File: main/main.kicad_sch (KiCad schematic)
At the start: 5 parts, among them SW1 SW_DPST_x2

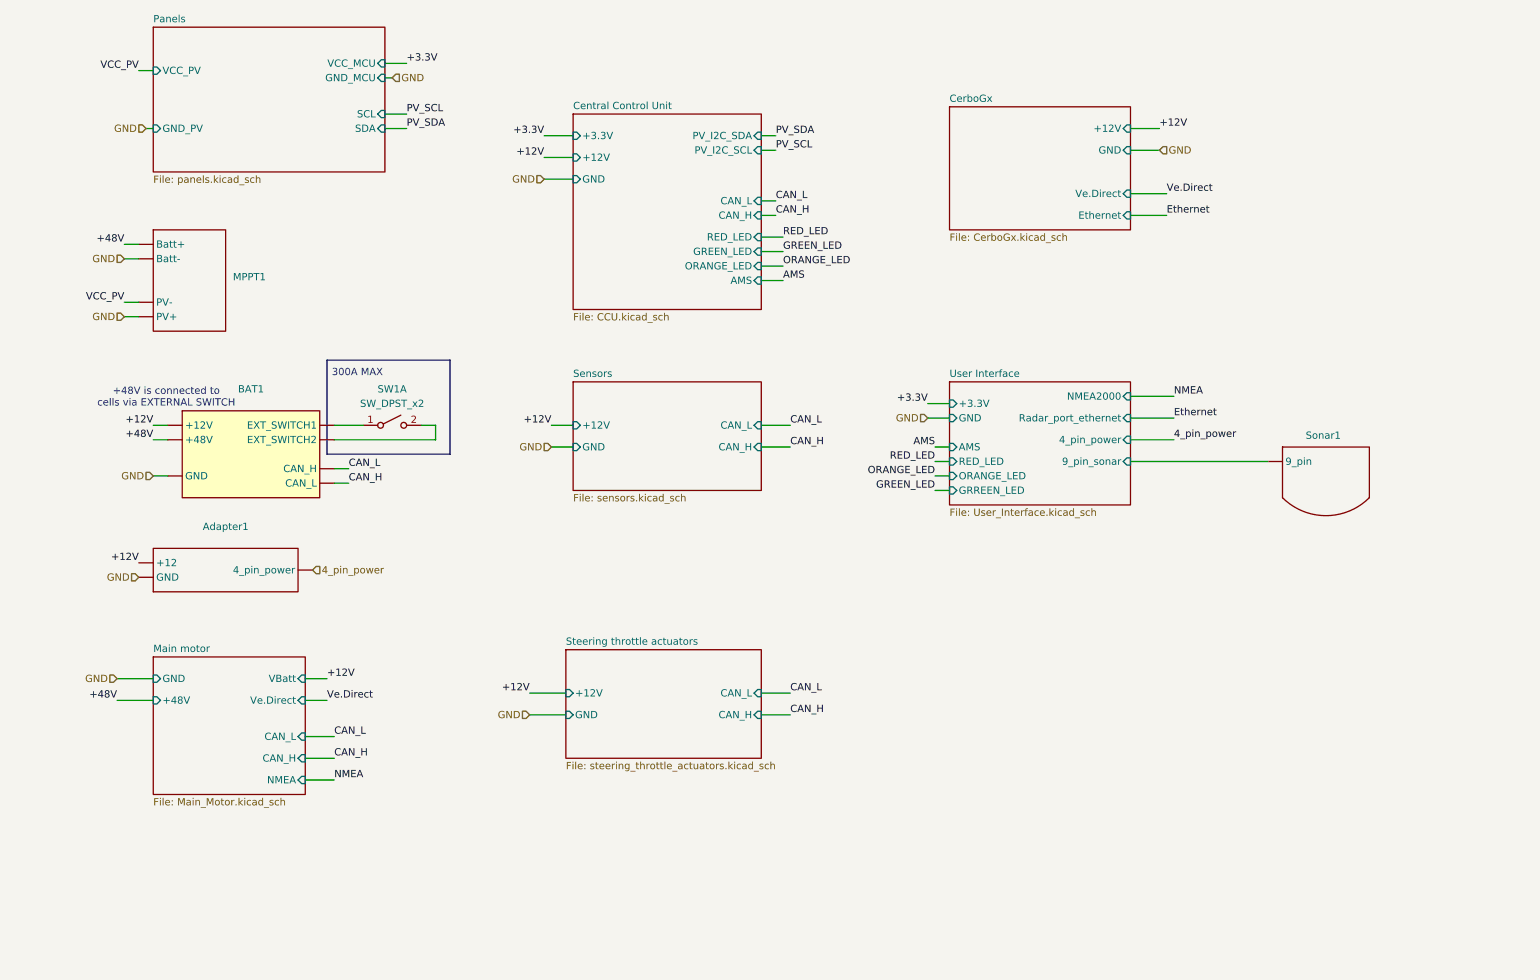
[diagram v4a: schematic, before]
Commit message: added emergency switch to mppt updateg seet layout
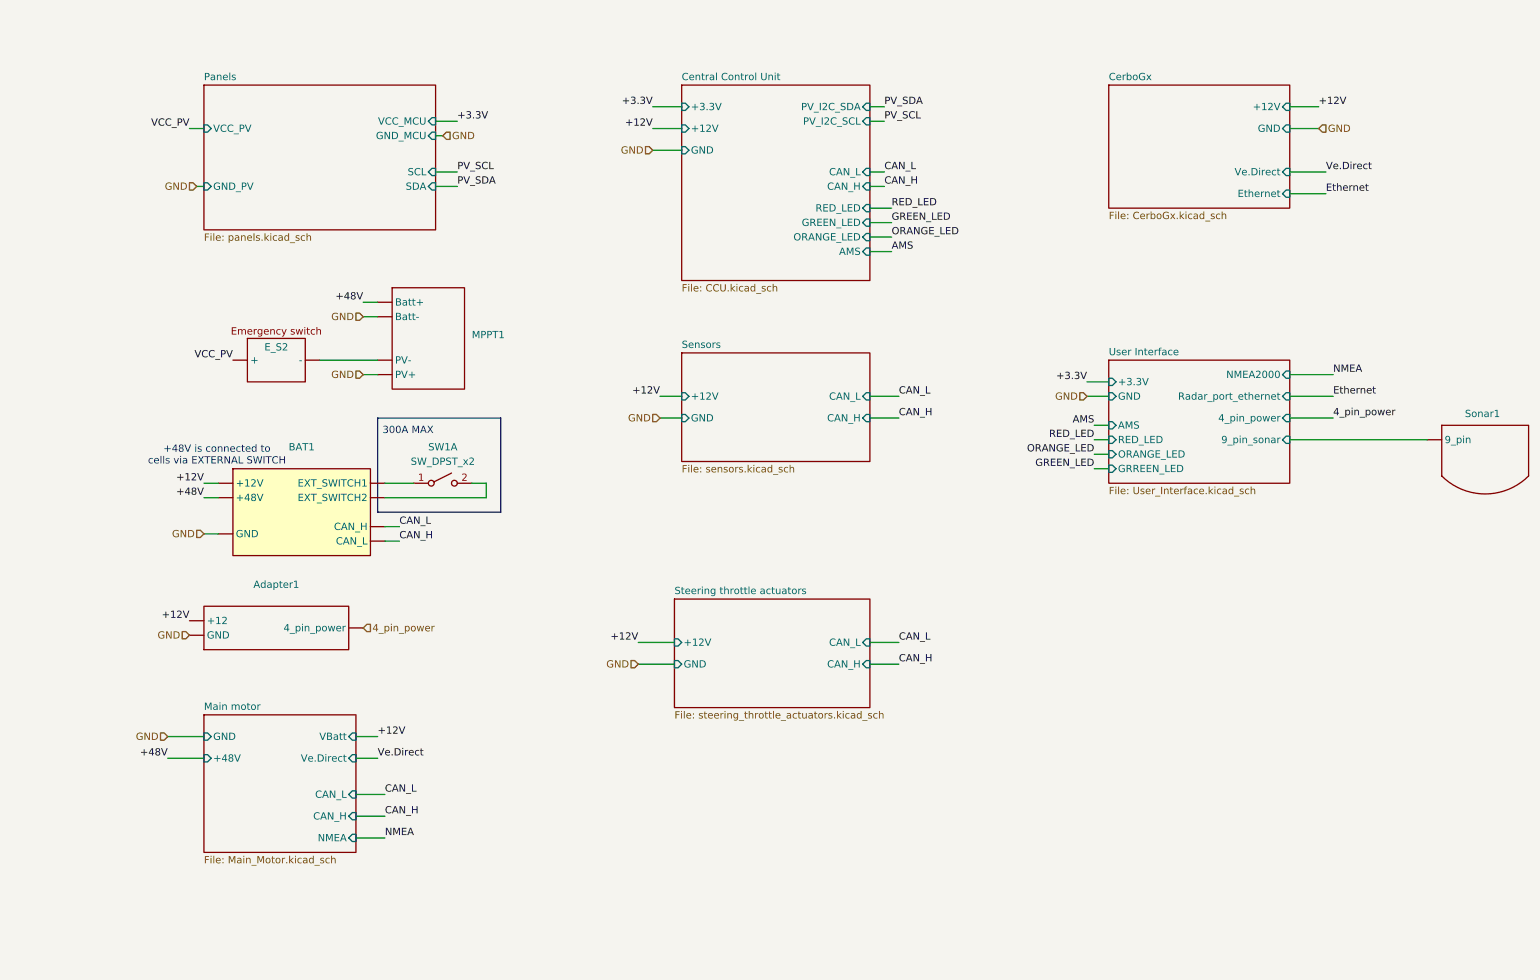
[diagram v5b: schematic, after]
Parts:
- added E_S2: ~, symbol New_Library_0:Emergency_Switch
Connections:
- net VCC_PV: now also E_S2. (-); no longer MPPT1. (PV-)
- new net: E_S2. (-), MPPT1. (PV-)
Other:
- moved on the sheet: Adapter1, BAT1, MPPT1, SW1A, Sonar1

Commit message: added logos, oranised sheets, final version
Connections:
- new net: E_S2. (-), MPPT1. (PV-)
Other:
- sheet User Interface ports: added Radar; removed Radar_port_ethernet
- company: (none) -> Designers: Krzysztof Grajek, Wojtek Kołodziej
- title: (none) -> POWERBoat Schematic
- moved on the sheet: Adapter1, BAT1, E_S2, MPPT1, SW1A, Sonar1

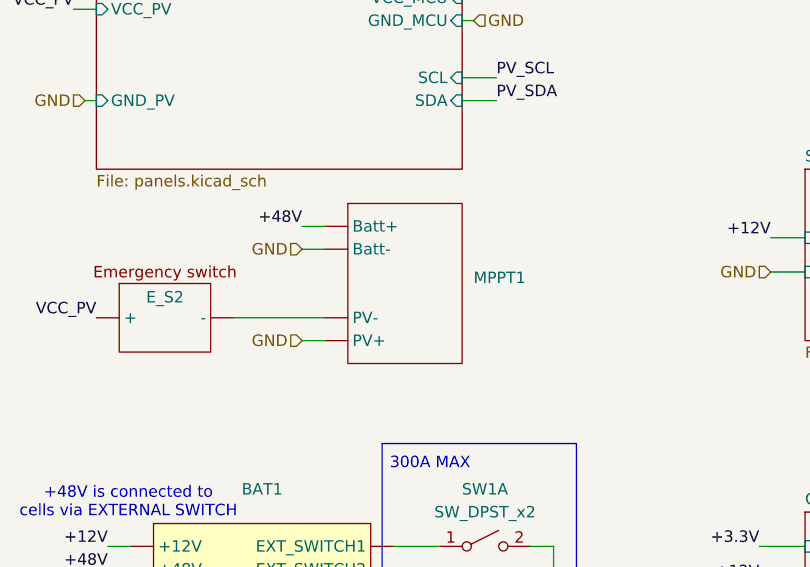
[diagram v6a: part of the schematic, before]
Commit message: Changed bg color of MPPT
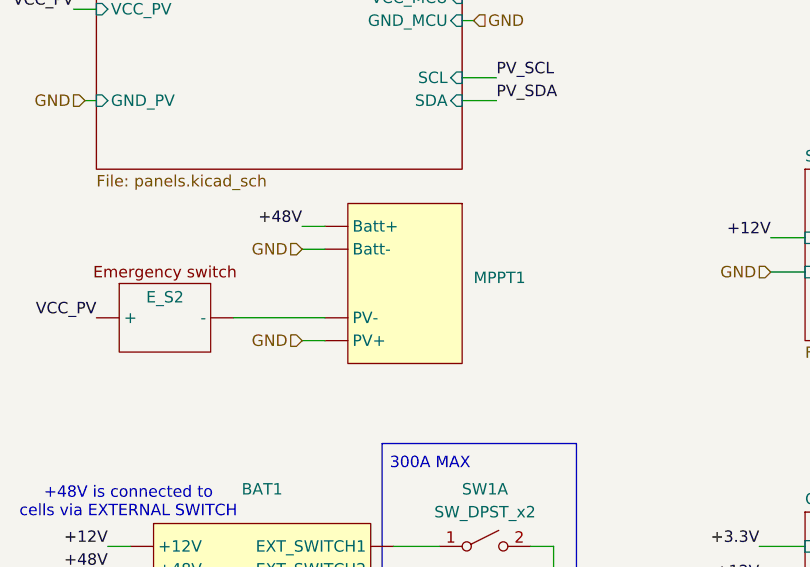
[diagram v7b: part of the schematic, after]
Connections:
- new net: E_S2. (-), MPPT1. (PV-)

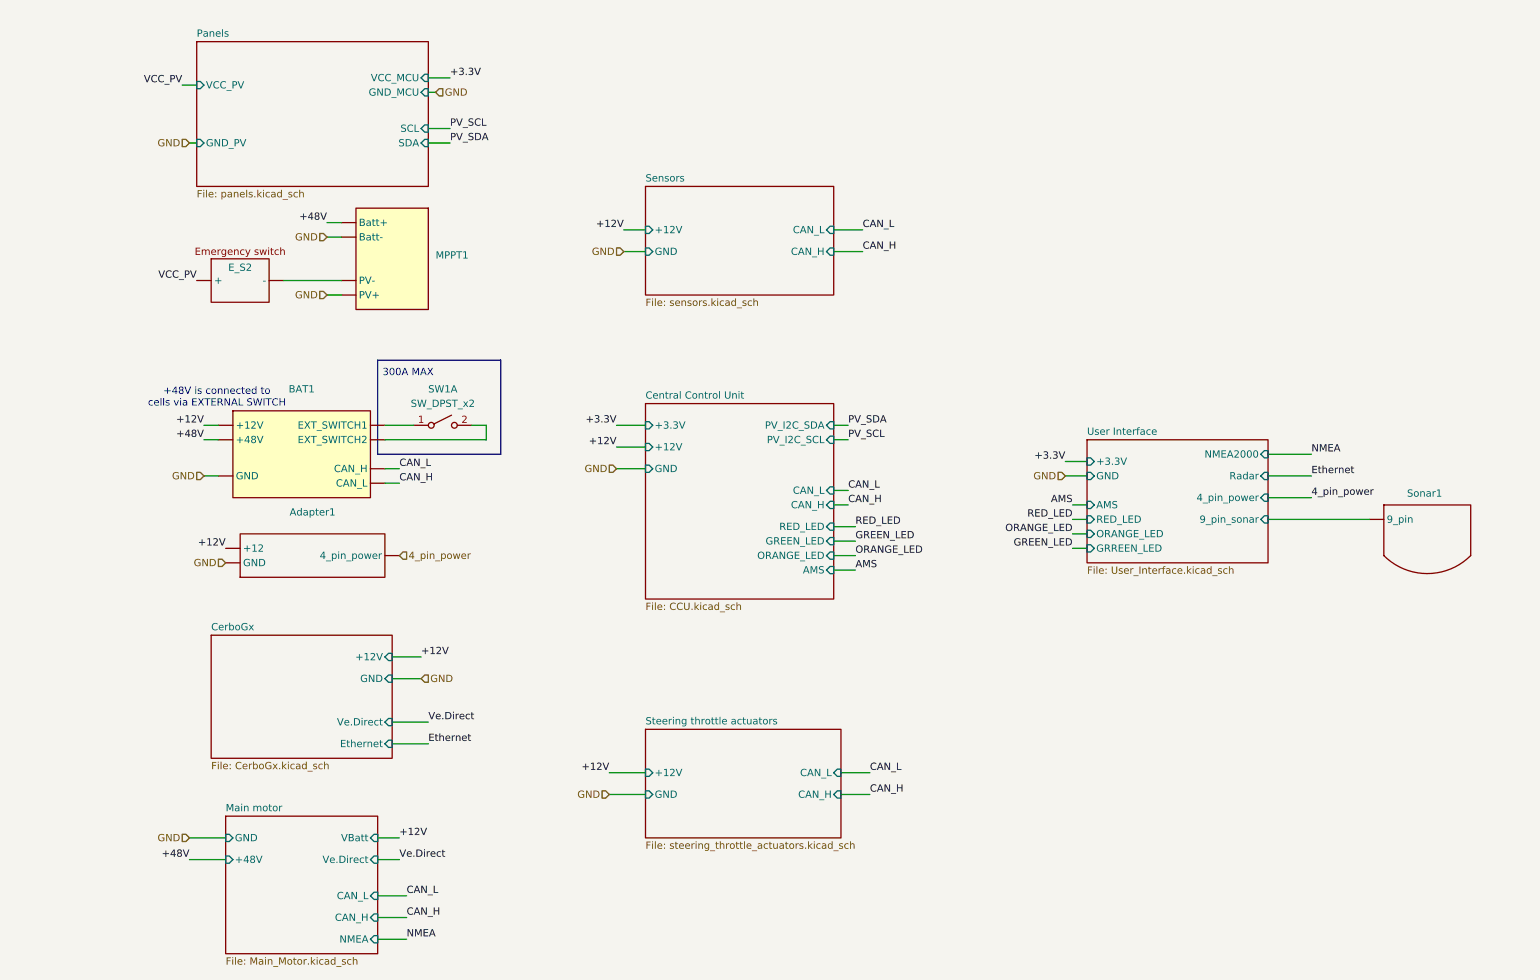
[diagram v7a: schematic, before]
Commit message: added nwe sheet (switching system), created a few new symbols, changed +48V coming from battery to Battery_High_voltage,
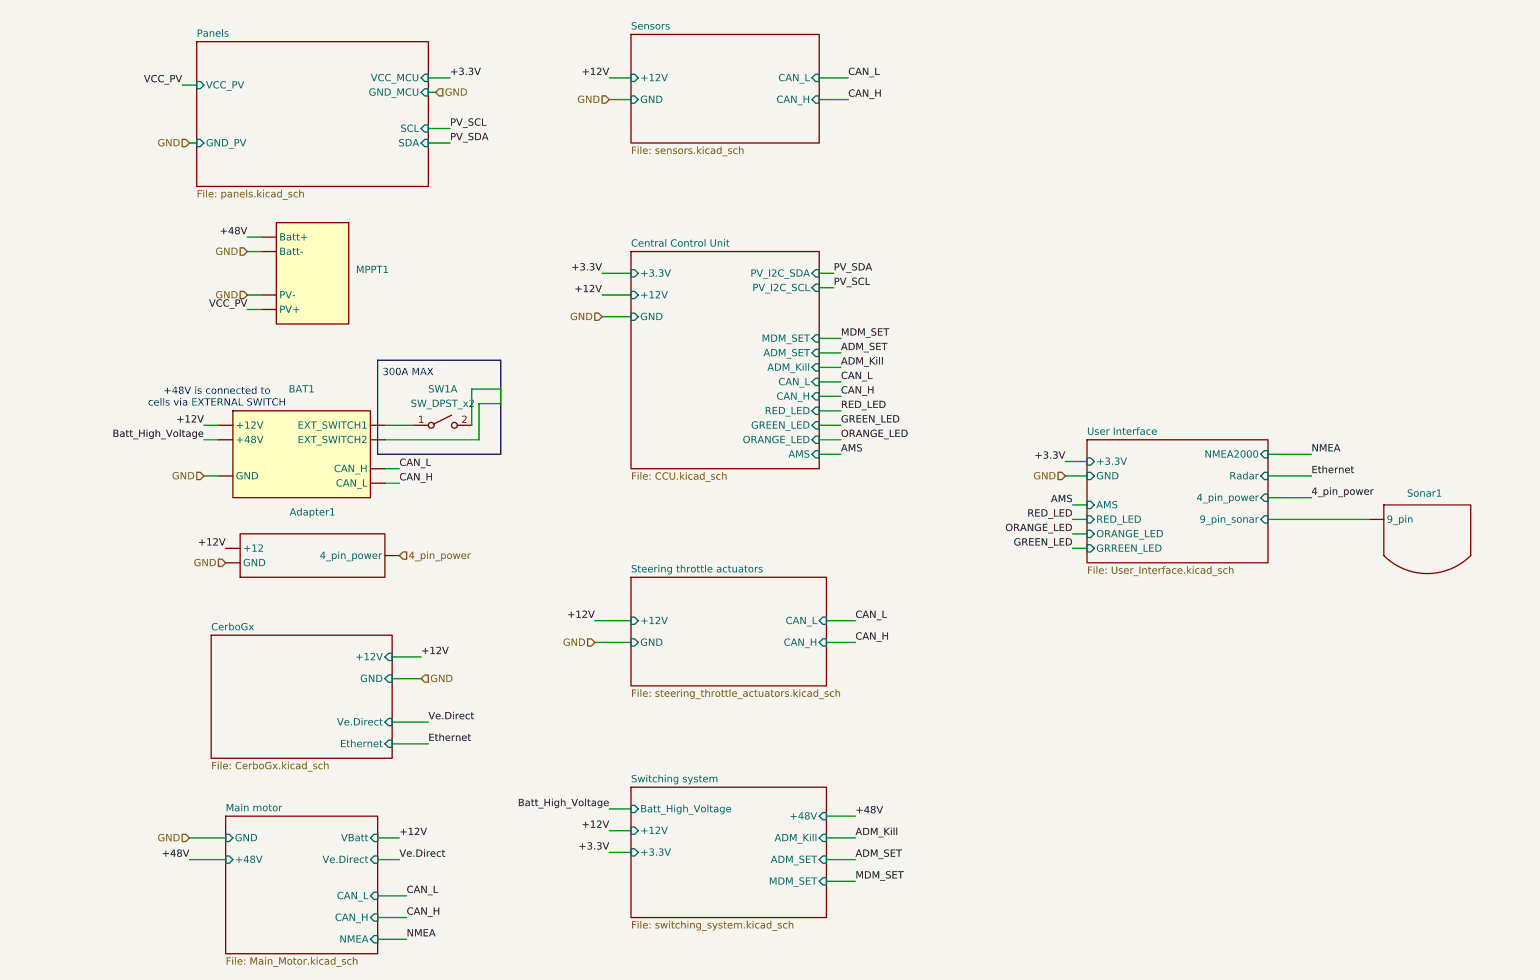
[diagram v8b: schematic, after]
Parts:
- removed E_S2: ~, symbol New_Library_0:Emergency_Switch
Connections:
- net +48V: no longer BAT1. (GND)
- net VCC_PV: now also MPPT1. (PV-)
- new net Batt_High_Voltage: BAT1. (GND)
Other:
- added sheet Switching system (switching_system.kicad_sch)
- sheet Central Control Unit ports: added ADM_Kill, ADM_SET, MDM_SET; removed none
- moved on the sheet: MPPT1
